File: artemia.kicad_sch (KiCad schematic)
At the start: 4 parts

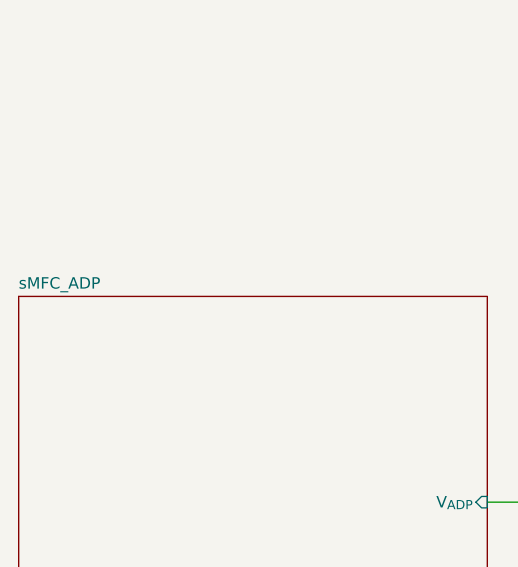
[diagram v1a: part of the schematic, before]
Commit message: Fix BSS123 pins, remove R18 R19 pulldowns
 - BSS123 pinout were completely wrong due to using the wrong symbol in
   the schematic. Made a new symbol with the right pinout. Fixes #7.
 - R18 and R19 were forming a voltage divider as V_GOOD and EN_PULSE
   are open-drain lines. Remove the pull-downs, and pray that circuit
   initialization is sane. Fixes #6.
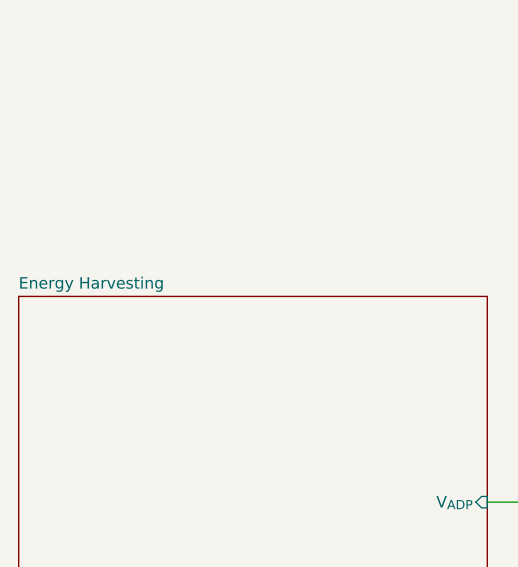
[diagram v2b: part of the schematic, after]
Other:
- sheet sMFC_ADP renamed Energy Harvesting
- title: Artemia -> Artemia: Power Management Subsystem
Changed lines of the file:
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@@
 	(paper "USLetter")
 	(title_block
-		(title "Artemia")
-		(date "2024-04-21")
-		(rev "A")
+		(title "Artemia: Power Management Subsystem")
+		(date "2024-11-21")
+		(rev "B*")
 		(company "UC San Diego")
 		(comment 1 "Author: ${AUTHOR}")
@@
 			(color 0 0 0 0.0000)
 		)
-		(property "Sheetname" "sMFC_ADP"
+		(property "Sheetname" "Energy Harvesting"
 			(at 31.75 64.0584 0)
 			(effects
